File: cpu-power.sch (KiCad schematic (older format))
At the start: 2 parts

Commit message: update power mark,
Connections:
- net labels added: VCC-IO
- net labels removed: Vcc-io
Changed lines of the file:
@@
 $Descr A3 16535 11693
 encoding utf-8
-Sheet 15 33
+Sheet 15 34
 Title ""
 Date ""
@@
 AR Path="/5C660882/5C614B67" Ref="U?"  Part="14"
 AR Path="/5C273FE9/5C291027/5C614B67" Ref="U?"  Part="14"
+AR Path="/5C7B767A/5C291027/5C614B67" Ref="U?"  Part="14"
 F 0 "U?" H 8150 7350 50  0000 C CNN
 F 1 "allwinner-H3" H 8150 7250 50  0000 C CNN
@@
 	1    0    0    -1
 $EndComp
-$Comp
-L taobao-components:Vcc-io #PWR?
-U 1 1 5C647B7D
-P 9400 6350
-AR Path="/5C5C55F2/5C647B7D" Ref="#PWR?"  Part="1"
-AR Path="/5C660882/5C647B7D" Ref="#PWR?"  Part="1"
-AR Path="/5C273FE9/5C291027/5C647B7D" Ref="#PWR?"  Part="1"
-F 0 "#PWR?" H 9400 6200 50  0001 C CNN
-F 1 "Vcc-io" H 9450 6500 50  0000 C CNN
-F 2 "" H 9400 6350 50  0001 C CNN
-F 3 "" H 9400 6350 50  0001 C CNN
-	1    9400 6350
-	1    0    0    -1
-$EndComp
 Wire Wire Line
 	9200 6400 9000 6400
@@
 AR Path="/5C660882/5C64CFBD" Ref="#PWR?"  Part="1"
 AR Path="/5C273FE9/5C291027/5C64CFBD" Ref="#PWR?"  Part="1"
+AR Path="/5C7B767A/5C291027/5C64CFBD" Ref="#PWR?"  Part="1"
 F 0 "#PWR?" H 9400 5000 50  0001 C CNN
 F 1 "Vdd-1V2-sys" H 9450 5300 50  0000 C CNN
@@
 AR Path="/5C660882/5C65652D" Ref="#PWR?"  Part="1"
 AR Path="/5C273FE9/5C291027/5C65652D" Ref="#PWR?"  Part="1"
+AR Path="/5C7B767A/5C291027/5C65652D" Ref="#PWR?"  Part="1"
 F 0 "#PWR?" H 6950 5000 50  0001 C CNN
 F 1 "VDD-CPUX" H 7000 5300 50  0000 C CNN
@@
 AR Path="/5C660882/5C6598C1" Ref="#PWR?"  Part="1"
 AR Path="/5C273FE9/5C291027/5C6598C1" Ref="#PWR?"  Part="1"
+AR Path="/5C7B767A/5C291027/5C6598C1" Ref="#PWR?"  Part="1"
 F 0 "#PWR?" H 6650 6300 50  0001 C CNN
 F 1 "VDD-CPUS" H 6700 6600 50  0000 C CNN
@@
 AR Path="/5C660882/5C65C4E7" Ref="C?"  Part="1"
 AR Path="/5C273FE9/5C291027/5C65C4E7" Ref="C?"  Part="1"
+AR Path="/5C7B767A/5C291027/5C65C4E7" Ref="C?"  Part="1"
 F 0 "C?" H 6750 6900 50  0000 L CNN
 F 1 "C105,0603" H 6750 6850 50  0000 L CNN
@@
 AR Path="/5C660882/5C65DD66" Ref="#PWR?"  Part="1"
 AR Path="/5C273FE9/5C291027/5C65DD66" Ref="#PWR?"  Part="1"
+AR Path="/5C7B767A/5C291027/5C65DD66" Ref="#PWR?"  Part="1"
 F 0 "#PWR?" H 6650 6850 50  0001 C CNN
 F 1 "GND" H 6700 6900 50  0000 C CNN
@@
 EndData
 $EndBitmap
+$Comp
+L taobao-components:VCC-IO #PWR?
+U 1 1 5C7D8805
+P 9400 6350
+F 0 "#PWR?" H 9400 6200 50  0001 C CNN
+F 1 "VCC-IO" H 9450 6500 50  0000 C CNN
+F 2 "" H 9400 6350 50  0001 C CNN
+F 3 "" H 9400 6350 50  0001 C CNN
+	1    9400 6350
+	1    0    0    -1
+$EndComp
 $EndSCHEMATC

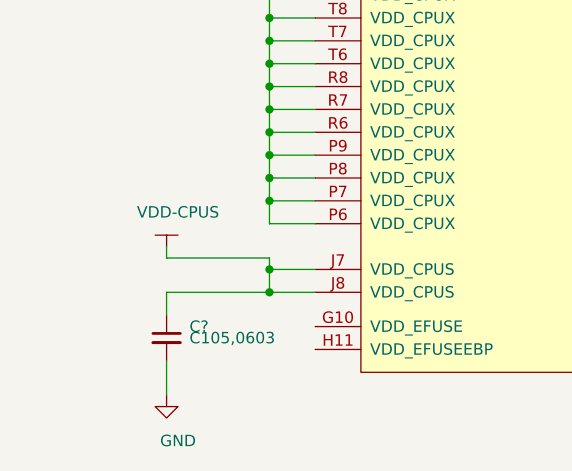
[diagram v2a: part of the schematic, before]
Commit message: update fix efuse circuit,
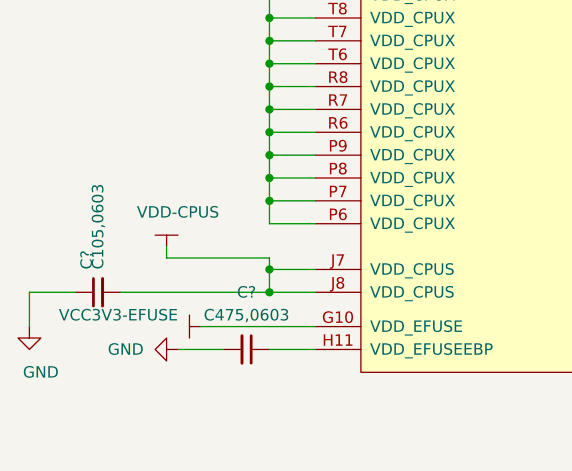
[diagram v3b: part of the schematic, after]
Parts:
- added C?: C475,0603, Capacitor_SMD:C_0603_1608Metric_Pad1.05x0.95mm_HandSolder, symbol taobao-c:C475,0603
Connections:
- net GND: now also C?.1, C?.2; no longer C?.2
- net VDD-CPUS: now also C?.2; no longer C?.1
- net VCC3V3-EFUSE: now reaches U?.G10 (VDD_EFUSE)
- net at U?.H11 (VDD_EFUSEEBP): now also C?.1
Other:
- moved on the sheet: C?
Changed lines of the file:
@@
 $Descr A3 16535 11693
 encoding utf-8
-Sheet 15 34
+Sheet 16 34
 Title ""
 Date ""
@@
 L taobao-c:C105,0603 C?
 U 1 1 5C65C4E7
-P 6650 6850
+P 6350 6650
 AR Path="/5C5C55F2/5C65C4E7" Ref="C?"  Part="1"
 AR Path="/5C660882/5C65C4E7" Ref="C?"  Part="1"
 AR Path="/5C273FE9/5C291027/5C65C4E7" Ref="C?"  Part="1"
 AR Path="/5C7B767A/5C291027/5C65C4E7" Ref="C?"  Part="1"
-F 0 "C?" H 6750 6900 50  0000 L CNN
-F 1 "C105,0603" H 6750 6850 50  0000 L CNN
-F 2 "Capacitor_SMD:C_0603_1608Metric_Pad1.05x0.95mm_HandSolder" H 6650 6850 50  0001 C CNN
-F 3 "~" H 6650 6850 50  0001 C CNN
-	1    6650 6850
-	1    0    0    -1
+F 0 "C?" H 6450 6700 50  0000 L CNN
+F 1 "C105,0603" H 6450 6650 50  0000 L CNN
+F 2 "Capacitor_SMD:C_0603_1608Metric_Pad1.05x0.95mm_HandSolder" H 6350 6650 50  0001 C CNN
+F 3 "~" H 6350 6650 50  0001 C CNN
+	1    6350 6650
+	0    -1   -1   0
 $EndComp
-Wire Wire Line
-	6650 6750 6650 6650
-Wire Wire Line
-	6650 6650 7100 6650
 Connection ~ 7100 6650
 $Comp
 L power:GND #PWR?
 U 1 1 5C65DD66
-P 6650 7100
+P 6050 6800
 AR Path="/5C5C55F2/5C65DD66" Ref="#PWR?"  Part="1"
 AR Path="/5C660882/5C65DD66" Ref="#PWR?"  Part="1"
 AR Path="/5C273FE9/5C291027/5C65DD66" Ref="#PWR?"  Part="1"
 AR Path="/5C7B767A/5C291027/5C65DD66" Ref="#PWR?"  Part="1"
-F 0 "#PWR?" H 6650 6850 50  0001 C CNN
-F 1 "GND" H 6700 6900 50  0000 C CNN
-F 2 "" H 6650 7100 50  0001 C CNN
-F 3 "" H 6650 7100 50  0001 C CNN
-	1    6650 7100
+F 0 "#PWR?" H 6050 6550 50  0001 C CNN
+F 1 "GND" H 6100 6600 50  0000 C CNN
+F 2 "" H 6050 6800 50  0001 C CNN
+F 3 "" H 6050 6800 50  0001 C CNN
+	1    6050 6800
 	1    0    0    -1
 $EndComp
 Wire Wire Line
-	6650 7100 6650 6950
+	6050 6800 6050 6650
 $Bitmap
 Pos 7950 3200
@@
 	1    0    0    -1
 $EndComp
+$Comp
+L taobao-components:VCC3V3-EFUSE #PWR?
+U 1 1 5C2F8ABE
+P 6800 6800
+F 0 "#PWR?" H 6800 6650 50  0001 C CNN
+F 1 "VCC3V3-EFUSE" V 6850 6900 50  0000 L CNN
+F 2 "" H 6800 6800 50  0001 C CNN
+F 3 "" H 6800 6800 50  0001 C CNN
+	1    6800 6800
+	0    -1   -1   0
+$EndComp
+Wire Wire Line
+	6450 6650 7100 6650
+Wire Wire Line
+	6250 6650 6050 6650
+$Comp
+L taobao-c:C475,0603 C?
+U 1 1 5C2FD674
+P 7000 6900
+F 0 "C?" V 6750 6900 50  0000 C CNN
+F 1 "C475,0603" V 6850 6900 50  0000 C CNN
+F 2 "Capacitor_SMD:C_0603_1608Metric_Pad1.05x0.95mm_HandSolder" H 7000 6900 50  0001 C CNN
+F 3 "~" H 7000 6900 50  0001 C CNN
+	1    7000 6900
+	0    1    1    0
+$EndComp
+$Comp
+L power:GND #PWR?
+U 1 1 5C2FD702
+P 6700 6900
+F 0 "#PWR?" H 6700 6650 50  0001 C CNN
+F 1 "GND" V 6700 6750 50  0000 R CNN
+F 2 "" H 6700 6900 50  0001 C CNN
+F 3 "" H 6700 6900 50  0001 C CNN
+	1    6700 6900
+	0    1    1    0
+$EndComp
+Wire Wire Line
+	6700 6900 6900 6900
+Wire Wire Line
+	7100 6900 7300 6900
+Wire Wire Line
+	6800 6800 7300 6800
 $EndSCHEMATC

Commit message: update,
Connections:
- net GND: now also C?.2; no longer C?.1
- net VDD-CPUS: now also C?.1; no longer C?.2
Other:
- moved on the sheet: C?
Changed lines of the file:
@@
 L taobao-components:VDD-CPUS #PWR?
 U 1 1 5C6598C1
-P 6650 6450
+P 6350 6450
 AR Path="/5C5C55F2/5C6598C1" Ref="#PWR?"  Part="1"
 AR Path="/5C660882/5C6598C1" Ref="#PWR?"  Part="1"
 AR Path="/5C273FE9/5C291027/5C6598C1" Ref="#PWR?"  Part="1"
 AR Path="/5C7B767A/5C291027/5C6598C1" Ref="#PWR?"  Part="1"
-F 0 "#PWR?" H 6650 6300 50  0001 C CNN
-F 1 "VDD-CPUS" H 6700 6600 50  0000 C CNN
-F 2 "" H 6650 6450 50  0001 C CNN
-F 3 "" H 6650 6450 50  0001 C CNN
-	1    6650 6450
+F 0 "#PWR?" H 6350 6300 50  0001 C CNN
+F 1 "VDD-CPUS" H 6400 6600 50  0000 C CNN
+F 2 "" H 6350 6450 50  0001 C CNN
+F 3 "" H 6350 6450 50  0001 C CNN
+	1    6350 6450
 	1    0    0    -1
 $EndComp
 Wire Wire Line
-	6650 6450 6650 6500
-Wire Wire Line
-	6650 6500 7100 6500
-Wire Wire Line
-	7100 6500 7100 6550
-Wire Wire Line
 	7100 6650 7300 6650
 Wire Wire Line
 	7300 6550 7100 6550
-Connection ~ 7100 6550
 Wire Wire Line
 	7100 6550 7100 6650
@@
 L taobao-c:C105,0603 C?
 U 1 1 5C65C4E7
-P 6350 6650
+P 6350 6900
 AR Path="/5C5C55F2/5C65C4E7" Ref="C?"  Part="1"
 AR Path="/5C660882/5C65C4E7" Ref="C?"  Part="1"
 AR Path="/5C273FE9/5C291027/5C65C4E7" Ref="C?"  Part="1"
 AR Path="/5C7B767A/5C291027/5C65C4E7" Ref="C?"  Part="1"
-F 0 "C?" H 6450 6700 50  0000 L CNN
-F 1 "C105,0603" H 6450 6650 50  0000 L CNN
-F 2 "Capacitor_SMD:C_0603_1608Metric_Pad1.05x0.95mm_HandSolder" H 6350 6650 50  0001 C CNN
-F 3 "~" H 6350 6650 50  0001 C CNN
-	1    6350 6650
-	0    -1   -1   0
+F 0 "C?" H 6250 6950 50  0000 R CNN
+F 1 "C105,0603" H 6250 6900 50  0000 R CNN
+F 2 "Capacitor_SMD:C_0603_1608Metric_Pad1.05x0.95mm_HandSolder" H 6350 6900 50  0001 C CNN
+F 3 "~" H 6350 6900 50  0001 C CNN
+	1    6350 6900
+	1    0    0    -1
 $EndComp
 Connection ~ 7100 6650
@@
 L power:GND #PWR?
 U 1 1 5C65DD66
-P 6050 6800
+P 6350 7300
 AR Path="/5C5C55F2/5C65DD66" Ref="#PWR?"  Part="1"
 AR Path="/5C660882/5C65DD66" Ref="#PWR?"  Part="1"
 AR Path="/5C273FE9/5C291027/5C65DD66" Ref="#PWR?"  Part="1"
 AR Path="/5C7B767A/5C291027/5C65DD66" Ref="#PWR?"  Part="1"
-F 0 "#PWR?" H 6050 6550 50  0001 C CNN
-F 1 "GND" H 6100 6600 50  0000 C CNN
-F 2 "" H 6050 6800 50  0001 C CNN
-F 3 "" H 6050 6800 50  0001 C CNN
-	1    6050 6800
+F 0 "#PWR?" H 6350 7050 50  0001 C CNN
+F 1 "GND" H 6400 7100 50  0000 C CNN
+F 2 "" H 6350 7300 50  0001 C CNN
+F 3 "" H 6350 7300 50  0001 C CNN
+	1    6350 7300
 	1    0    0    -1
 $EndComp
-Wire Wire Line
-	6050 6800 6050 6650
 $Bitmap
 Pos 7950 3200
@@
 	0    -1   -1   0
 $EndComp
-Wire Wire Line
-	6450 6650 7100 6650
-Wire Wire Line
-	6250 6650 6050 6650
 $Comp
 L taobao-c:C475,0603 C?
 U 1 1 5C2FD674
-P 7000 6900
-F 0 "C?" V 6750 6900 50  0000 C CNN
-F 1 "C475,0603" V 6850 6900 50  0000 C CNN
-F 2 "Capacitor_SMD:C_0603_1608Metric_Pad1.05x0.95mm_HandSolder" H 7000 6900 50  0001 C CNN
-F 3 "~" H 7000 6900 50  0001 C CNN
-	1    7000 6900
-	0    1    1    0
+P 6800 7150
+F 0 "C?" V 6950 7150 50  0000 C CNN
+F 1 "C475,0603" V 7050 7150 50  0000 C CNN
+F 2 "Capacitor_SMD:C_0603_1608Metric_Pad1.05x0.95mm_HandSolder" H 6800 7150 50  0001 C CNN
+F 3 "~" H 6800 7150 50  0001 C CNN
+	1    6800 7150
+	1    0    0    -1
 $EndComp
 $Comp
 L power:GND #PWR?
 U 1 1 5C2FD702
-P 6700 6900
-F 0 "#PWR?" H 6700 6650 50  0001 C CNN
-F 1 "GND" V 6700 6750 50  0000 R CNN
-F 2 "" H 6700 6900 50  0001 C CNN
-F 3 "" H 6700 6900 50  0001 C CNN
-	1    6700 6900
-	0    1    1    0
+P 6800 7450
+F 0 "#PWR?" H 6800 7200 50  0001 C CNN
+F 1 "GND" V 6800 7300 50  0000 R CNN
+F 2 "" H 6800 7450 50  0001 C CNN
+F 3 "" H 6800 7450 50  0001 C CNN
+	1    6800 7450
+	1    0    0    -1
 $EndComp
 Wire Wire Line
-	6700 6900 6900 6900
-Wire Wire Line
-	7100 6900 7300 6900
+	6800 7450 6800 7250
 Wire Wire Line
 	6800 6800 7300 6800
+Wire Wire Line
+	6800 7050 6800 6900
+Wire Wire Line
+	6800 6900 7300 6900
+Wire Wire Line
+	6350 7000 6350 7300
+Wire Wire Line
+	6350 6800 6350 6650
+Wire Wire Line
+	6350 6650 7100 6650
+Wire Wire Line
+	6350 6450 6350 6650
+Connection ~ 6350 6650
 $EndSCHEMATC
